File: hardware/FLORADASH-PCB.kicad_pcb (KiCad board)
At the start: 4 copper layers, 139.5 x 50.9 mm, 95 parts, among them IC1 LM66200DRLR, J1 USB_C_Receptacle_USB2.0_16P, J2 Conn_01x04_Pin, J3 Conn_02x04_Top_Bottom, Q1 FS8205, Q2 FS8205, SW1 SW_Push, SW2 SW_Push, U1 TP4056-42-ESOP8, U2 USBLC6-2SC6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

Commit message: finish the first routing
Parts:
- removed H4: MountingHole, MountingHole:MountingHole_2.2mm_M2_DIN965_Pad
- added H3: MountingHole, MountingHole:MountingHole_2.2mm_M2_DIN965_Pad, F.Cu at (192.0, 136.0)
- moved TP2 3.72 mm to (123.8, 106.0)
- moved TP5 2.36 mm to (192.5, 103.2)
- moved C1 1.36 mm to (120.2, 109.8)
- moved C2 1.36 mm to (123.8, 109.8)
- moved L1 1.36 mm to (122.0, 109.8)
- moved D1 1.07 mm to (119.8, 97.2)
- moved C15 0.75 mm to (180.2, 118.2)
- moved R1 0.57 mm to (117.5, 97.2)
- moved TP1 0.50 mm to (114.8, 108.5)
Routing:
- net D+: track 0.00 -> 81.1 mm, vias 0 -> 2
- net D-: track 0.00 -> 80.8 mm, vias 0 -> 2
- net TX: track 0.00 -> 59.2 mm, vias 0 -> 2
- net RX: track 0.00 -> 59.1 mm, vias 0 -> 2
- net GND: track 1.37 -> 35.4 mm, vias 1 -> 3
- net Net-(U3-OD): track 6.54 -> 17.8 mm, vias 0 -> 2
- net +3.3V: track 202.9 -> 209.1 mm, vias 0 -> 2
- net TO_CAP_PLATE: track 0.00 -> 5.27 mm
- net +5V: track 21.5 -> 26.6 mm
- net Net-(U1-PROG): track 0.00 -> 2.39 mm
- net Net-(J1-D+-PadA6): track 6.04 -> 8.14 mm
- net Bat+: track 48.1 -> 46.4 mm
- net Bat-: track 123.7 -> 122.6 mm
- net Net-(IC1-ST): track 1.25 -> 1.82 mm
- net Net-(D1-A): track 1.78 -> 2.28 mm

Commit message: PCB customization
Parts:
- removed the G*** at (228.6, 107.3)
- removed the G*** at (228.6, 119.0)
- removed kibuzzard-693B565E (x2): G***, kibuzzard-693B565E
- removed kibuzzard-6969377A: G***, kibuzzard-6969377A
- removed kibuzzard-6969378A: G***, kibuzzard-6969378A
- removed kibuzzard-69693792: G***, kibuzzard-69693792
- removed kibuzzard-69693797: G***, kibuzzard-69693797
- removed kibuzzard-6969379D: G***, kibuzzard-6969379D
- removed kibuzzard-696937A1: G***, kibuzzard-696937A1
- removed kibuzzard-696937A5: G***, kibuzzard-696937A5
- added G***: LOGO, LOGO, F.Cu at (167.8, 134.8)
- added G***: LOGO, LOGO, F.Cu at (196.5, 111.0)
- added G***: LOGO, LOGO, F.Cu at (220.6, 113.1)
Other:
- board text added: "Capacitive soil mosture"

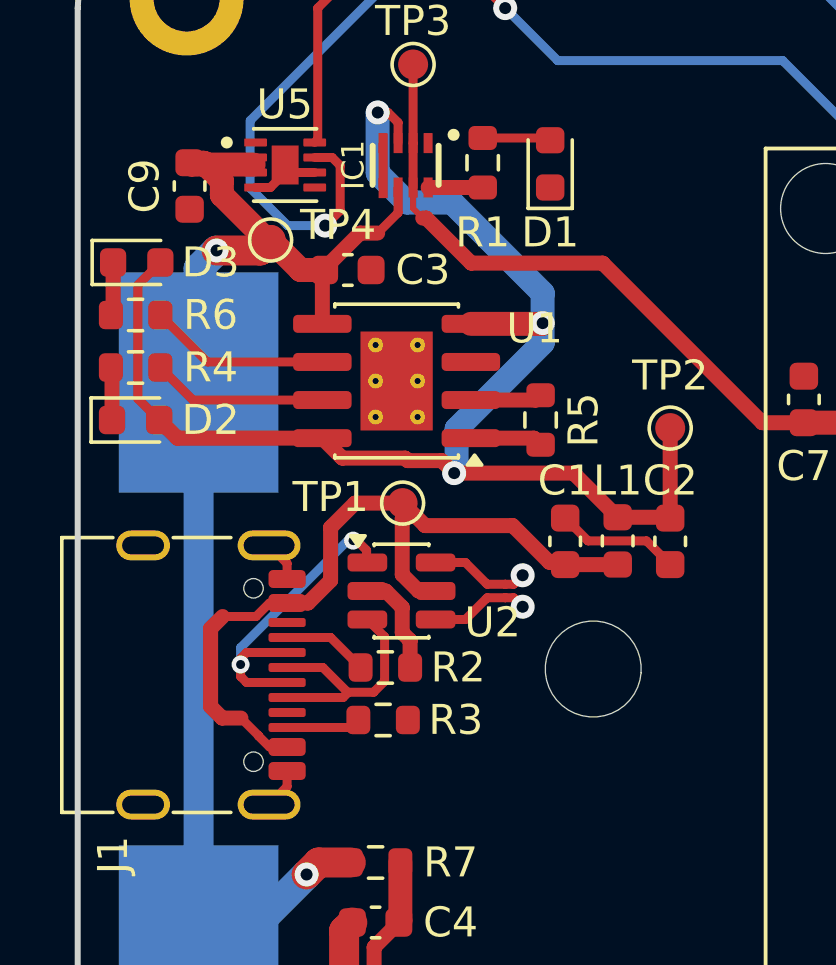
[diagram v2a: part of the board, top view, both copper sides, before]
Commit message: Fixed all DRC constraint
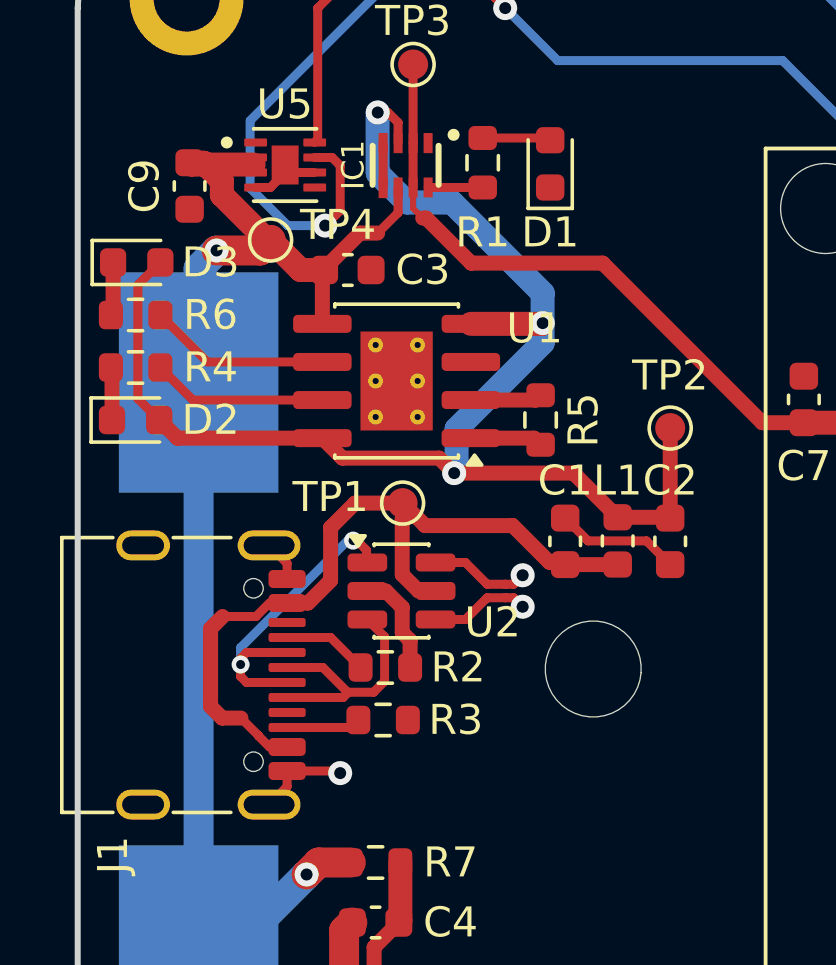
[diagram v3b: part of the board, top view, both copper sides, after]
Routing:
- net GND: track 35.4 -> 37.2 mm, vias 3 -> 4
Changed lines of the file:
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@@
 		)
 		(pad_to_mask_clearance 0)
+		(solder_mask_min_width 0.13)
 		(allow_soldermask_bridges_in_footprints no)
 		(tenting
@@
 			)
 		)
-		(attr smd)
+		(solder_mask_margin 0)
+		(solder_paste_margin 0)
+		(clearance 0)
+		(attr smd allow_soldermask_bridges)
 		(duplicate_pad_numbers_are_jumpers no)
 		(fp_line
@@
 			)
 		)
-		(attr smd)
+		(attr smd allow_soldermask_bridges)
 		(duplicate_pad_numbers_are_jumpers no)
 		(fp_line
@@
 		(at 148.885 114.03)
 		(property "Reference" "BT1"
-			(at 0 20.980433 0)
+			(at 0 20.980433 180)
 			(layer "B.SilkS")
 			(effects
@@
 		)
 		(property "Value" "~"
-			(at 0 -20.9505 0)
+			(at 0 -20.9505 180)
 			(layer "B.Fab")
 			(effects
@@
 		)
 		(property "Datasheet" ""
-			(at 0 0 0)
+			(at 0 0 180)
 			(layer "B.Fab")
 			(hide yes)
@@
 		)
 		(property "Description" ""
-			(at 0 0 0)
+			(at 0 0 180)
 			(layer "B.Fab")
 			(hide yes)
@@
 		(sheetname "/")
 		(sheetfile "FLORADASH-PCB.kicad_sch")
-		(units
-			(unit
-				(name "A")
-				(pins "1" "3" "2" "4")
-			)
-		)
 		(duplicate_pad_numbers_are_jumpers no)
 		(fp_line
@@
 			(layer "Edge.Cuts")
 		)
-		(fp_rect
-			(start -43.765 20.255433)
-			(end 43.765 -20.2255)
-			(stroke
-				(width 0.05)
-				(type default)
-			)
-			(fill no)
-			(layer "B.CrtYd")
-		)
 		(fp_line
 			(start -38.5 -19.95)
@@
 		)
 		(fp_text user "${REFERENCE}"
-			(at 0 0 0)
+			(at 0 0 180)
 			(layer "B.Fab")
 			(effects
@@
 	)
 	(segment
-		(start 110.98 117.95)
-		(end 110.38 118.55)
-		(width 0.3)
-		(layer "F.Cu")
-		(net "GND")
-	)
-	(segment
 		(start 114.8175 111.977316)
 		(end 114.8175 112.8175)
@@
 	)
 	(segment
+		(start 110.98 117.95)
+		(end 110.38 118.55)
+		(width 0.3)
+		(layer "F.Cu")
+		(net "GND")
+	)
+	(segment
 		(start 188.15 118.56)
 		(end 186.06 118.56)
@@
 	)
 	(segment
+		(start 112.68 117.43)
+		(end 112.75 117.5)
+		(width 0.3)
+		(layer "F.Cu")
+		(net "GND")
+	)
+	(segment
 		(start 121.0105 109.7605)
 		(end 122.9605 109.7605)
@@
 	)
 	(segment
+		(start 110.98 117.43)
+		(end 112.68 117.43)
+		(width 0.3)
+		(layer "F.Cu")
+		(net "GND")
+	)
+	(segment
 		(start 110.915 97.48614)
 		(end 110.915 97.23)
@@
 	)
 	(via
+		(at 112.75 117.5)
+		(size 0.8)
+		(drill 0.4)
+		(layers "F.Cu" "B.Cu")
+		(net "GND")
+	)
+	(via
 		(at 142 96.25)
 		(size 0.8)
@@
 	)
 	(segment
+		(start 115.18 97.98)
+		(end 115.18 96.5)
+		(width 0.3)
+		(layer "F.Cu")
+		(net "battery{slash}usb")
+	)
+	(segment
 		(start 126.82 105.82)
 		(end 128.205 105.82)
@@
 	)
 	(segment
-		(start 115.18 97.98)
-		(end 115.18 96.5)
-		(width 0.3)
-		(layer "F.Cu")
-		(net "battery{slash}usb")
-	)
-	(segment
 		(start 128.205 105.82)
 		(end 130.47 105.82)
@@
 	)
 	(segment
+		(start 116.05 107)
+		(end 112.82 107)
+		(width 0.5)
+		(layer "F.Cu")
+		(net "+5V_FILT")
+	)
+	(segment
 		(start 123.75 109)
 		(end 123.75 106)
@@
 	)
 	(segment
+		(start 116.55 107.5)
+		(end 116.05 107)
+		(width 0.5)
+		(layer "F.Cu")
+		(net "+5V_FILT")
+	)
+	(segment
 		(start 106.005 105.0175)
 		(end 106.005 101.23)
@@
 	)
 	(segment
-		(start 116.135 107.085)
-		(end 115 107.085)
-		(width 0.5)
-		(layer "F.Cu")
-		(net "+5V_FILT")
-	)
-	(segment
 		(start 122 108.973)
 		(end 123.723 108.973)
@@
 	)
 	(segment
-		(start 114.915 107)
-		(end 112.82 107)
-		(width 0.5)
-		(layer "F.Cu")
-		(net "+5V_FILT")
-	)
-	(segment
-		(start 112.82 107)
-		(end 112.155 106.335)
-		(width 0.5)
-		(layer "F.Cu")
-		(net "+5V_FILT")
-	)
-	(segment
-		(start 115 107.085)
-		(end 114.915 107)
-		(width 0.5)
-		(layer "F.Cu")
-		(net "+5V_FILT")
-	)
-	(segment
 		(start 119.475 102.525)
 		(end 117.105 102.525)
@@
 	)
 	(segment
-		(start 116.55 107.5)
-		(end 116.135 107.085)
-		(width 0.5)
-		(layer "F.Cu")
-		(net "+5V_FILT")
-	)
-	(segment
 		(start 114 95.48)
 		(end 114.345 95.48)
@@
 		(net "+5V_FILT")
 	)
+	(segment
+		(start 112.82 107)
+		(end 112.155 106.335)
+		(width 0.5)
+		(layer "F.Cu")
+		(net "+5V_FILT")
+	)
 	(via
 		(at 119.5 102.5)
@@
 	)
 	(segment
-		(start 115.68 97.98)
-		(end 117.5 97.98)
-		(width 0.5)
+		(start 117.5 97.98)
+		(end 115.68 97.98)
+		(width 0.3)
 		(layer "F.Cu")
 		(net "Net-(IC1-ST)")
@@
 		(priority 1)
 		(connect_pads
-			(clearance 0.1778)
+			(clearance 0.2)
 		)
 		(min_thickness 0.25)

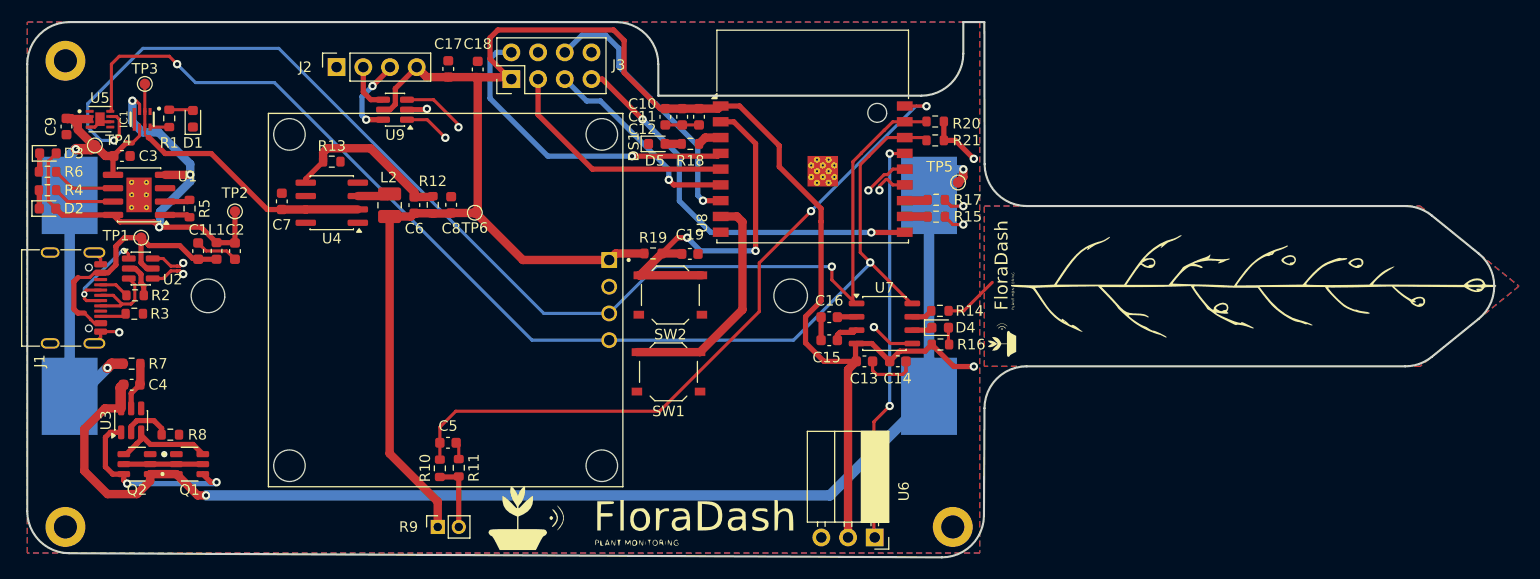
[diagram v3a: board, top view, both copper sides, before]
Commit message: Added the sillkcreen def
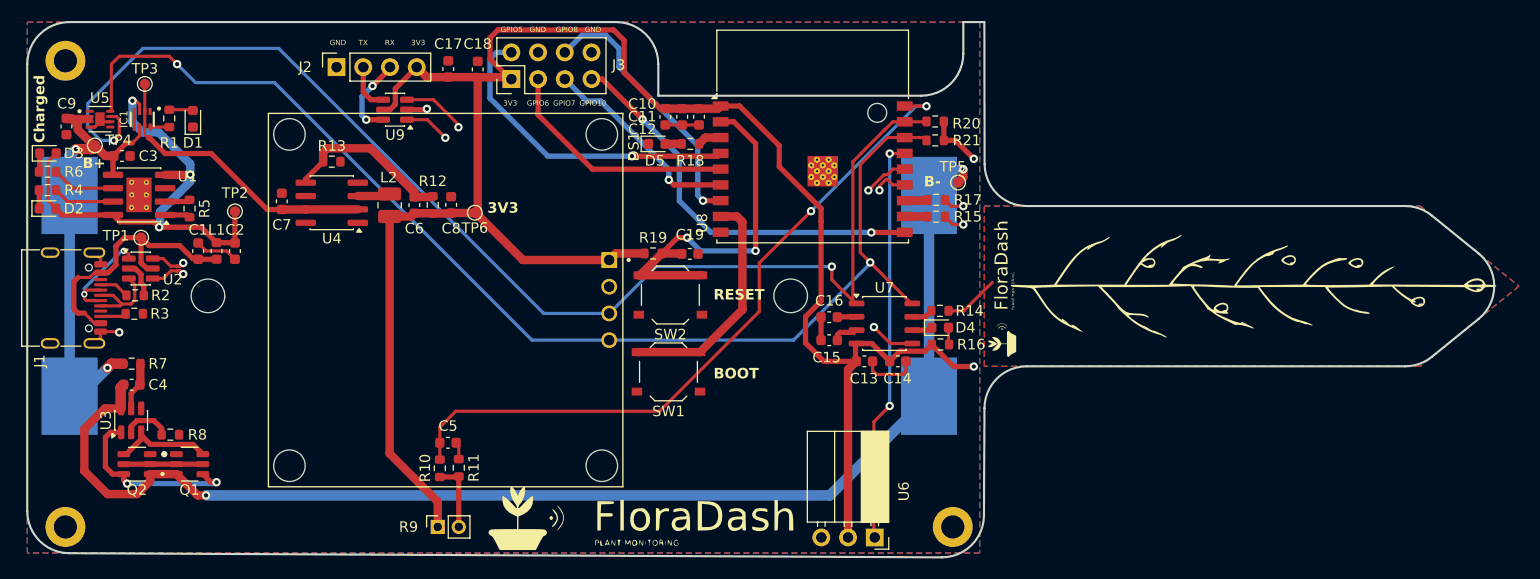
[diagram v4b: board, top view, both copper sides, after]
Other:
- board text added: "3V3"
- board text added: "B+"
- board text added: "B-"
- board text added: "BOOT"
- board text added: "Charged"
- board text added: "GND"
- board text added: "GPIO10"
- board text added: "GPIO5"
- board text added: "GPIO6"
- board text added: "GPIO7"
- board text added: "GPIO8"
- board text added: "RESET"
- board text added: "RX"
- board text added: "TX"
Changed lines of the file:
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@@
 		(tags "capacitor")
 		(property "Reference" "C9"
-			(at 0 1.5 90)
+			(at -2.18 -0.02 180)
 			(layer "F.SilkS")
 			(effects
@@
 		(tags "test point SMD pad")
 		(property "Reference" "TP5"
-			(at -1.75 -1.5 0)
+			(at -0.5 -1.5 0)
 			(layer "F.SilkS")
 			(effects
@@
 		)
 		(fp_text user "${REFERENCE}"
-			(at -1.75 -1.5 0)
+			(at -0.5 -1.5 0)
 			(layer "F.Fab")
 			(effects
@@
 		(layer "Edge.Cuts")
 	)
+	(gr_text "GND"
+		(at 132.75 90.25 0)
+		(layer "F.SilkS")
+		(effects
+			(font
+				(size 0.5 0.5)
+				(thickness 0.0375)
+			)
+			(justify left bottom)
+		)
+	)
+	(gr_text "TX"
+		(at 135.5 90.25 0)
+		(layer "F.SilkS")
+		(effects
+			(font
+				(size 0.5 0.5)
+				(thickness 0.0375)
+			)
+			(justify left bottom)
+		)
+	)
+	(gr_text "RX"
+		(at 138 90.25 0)
+		(layer "F.SilkS")
+		(effects
+			(font
+				(size 0.5 0.5)
+				(thickness 0.0375)
+			)
+			(justify left bottom)
+		)
+	)
+	(gr_text "3V3"
+		(at 140.5 90.25 0)
+		(layer "F.SilkS")
+		(effects
+			(font
+				(size 0.5 0.5)
+				(thickness 0.0375)
+			)
+			(justify left bottom)
+		)
+	)
+	(gr_text "GPIO5"
+		(at 149 89 0)
+		(layer "F.SilkS")
+		(effects
+			(font
+				(size 0.5 0.5)
+				(thickness 0.0375)
+			)
+			(justify left bottom)
+		)
+	)
+	(gr_text "3V3"
+		(at 149.25 96 0)
+		(layer "F.SilkS")
+		(effects
+			(font
+				(size 0.5 0.5)
+				(thickness 0.0375)
+			)
+			(justify left bottom)
+		)
+	)
+	(gr_text "GPIO6"
+		(at 151.5 96 0)
+		(layer "F.SilkS")
+		(effects
+			(font
+				(size 0.5 0.5)
+				(thickness 0.0375)
+			)
+			(justify left bottom)
+		)
+	)
+	(gr_text "GND"
+		(at 151.75 89 0)
+		(layer "F.SilkS")
+		(effects
+			(font
+				(size 0.5 0.5)
+				(thickness 0.0375)
+			)
+			(justify left bottom)
+		)
+	)
+	(gr_text "GPIO7"
+		(at 154 96 0)
+		(layer "F.SilkS")
+		(effects
+			(font
+				(size 0.5 0.5)
+				(thickness 0.0375)
+			)
+			(justify left bottom)
+		)
+	)
+	(gr_text "GPIO8"
+		(at 154.25 89 0)
+		(layer "F.SilkS")
+		(effects
+			(font
+				(size 0.5 0.5)
+				(thickness 0.0375)
+			)
+			(justify left bottom)
+		)
+	)
+	(gr_text "GPIO10"
+		(at 156.5 96 0)
+		(layer "F.SilkS")
+		(effects
+			(font
+				(size 0.5 0.5)
+				(thickness 0.0375)
+			)
+			(justify left bottom)
+		)
+	)
+	(gr_text "GND"
+		(at 157 89 0)
+		(layer "F.SilkS")
+		(effects
+			(font
+				(size 0.5 0.5)
+				(thickness 0.0375)
+			)
+			(justify left bottom)
+		)
+	)
+	(gr_text "B+"
+		(at 109.25 102 0)
+		(layer "F.SilkS")
+		(effects
+			(font
+				(size 1 1)
+				(thickness 0.25)
+				(bold yes)
+			)
+			(justify left bottom)
+		)
+	)
+	(gr_text "3V3"
+		(at 147.75 106.25 0)
+		(layer "F.SilkS")
+		(effects
+			(font
+				(size 1 1)
+				(thickness 0.25)
+				(bold yes)
+			)
+			(justify left bottom)
+		)
+	)
+	(gr_text "RESET"
+		(at 169.25 114.5 0)
+		(layer "F.SilkS")
+		(effects
+			(font
+				(size 1 1)
+				(thickness 0.25)
+				(bold yes)
+			)
+			(justify left bottom)
+		)
+	)
+	(gr_text "BOOT"
+		(at 169.25 122 0)
+		(layer "F.SilkS")
+		(effects
+			(font
+				(size 1 1)
+				(thickness 0.25)
+				(bold yes)
+			)
+			(justify left bottom)
+		)
+	)
+	(gr_text "B-"
+		(at 189.25 103.75 0)
+		(layer "F.SilkS")
+		(effects
+			(font
+				(size 1 1)
+				(thickness 0.25)
+				(bold yes)
+			)
+			(justify left bottom)
+		)
+	)
+	(gr_text "Charged"
+		(at 105.75 99.5 90)
+		(layer "F.SilkS")
+		(effects
+			(font
+				(size 1 1)
+				(thickness 0.25)
+				(bold yes)
+			)
+			(justify left bottom)
+		)
+	)
 	(gr_text "Capacitive soil mosture"

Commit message: Finished the footprint assignation and PCB
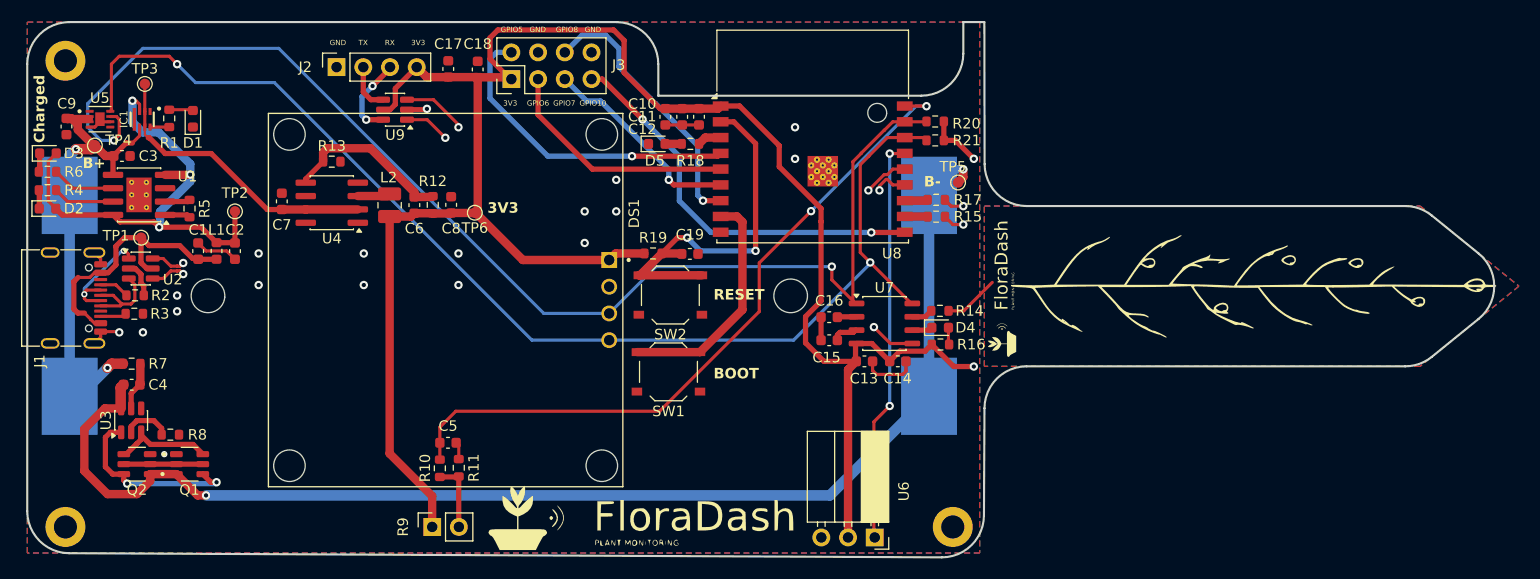
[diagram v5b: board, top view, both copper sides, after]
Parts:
- R9: footprint Connector_PinSocket_2.00mm:PinSocket_1x02_P2.00mm_Vertical -> Connector_PinSocket_2.54mm:PinSocket_1x02_P2.54mm_Vertical
- moved R9 0.53 mm to (142.5, 136.0)
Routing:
- net GND: vias 4 -> 19
- added copper zone on In1.Cu, net GND
- added copper zone on In2.Cu, net GND
